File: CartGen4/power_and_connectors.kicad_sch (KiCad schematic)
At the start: 34 parts, among them J2 Conn_01x05_Male, U1 TPS65266-1RHBR

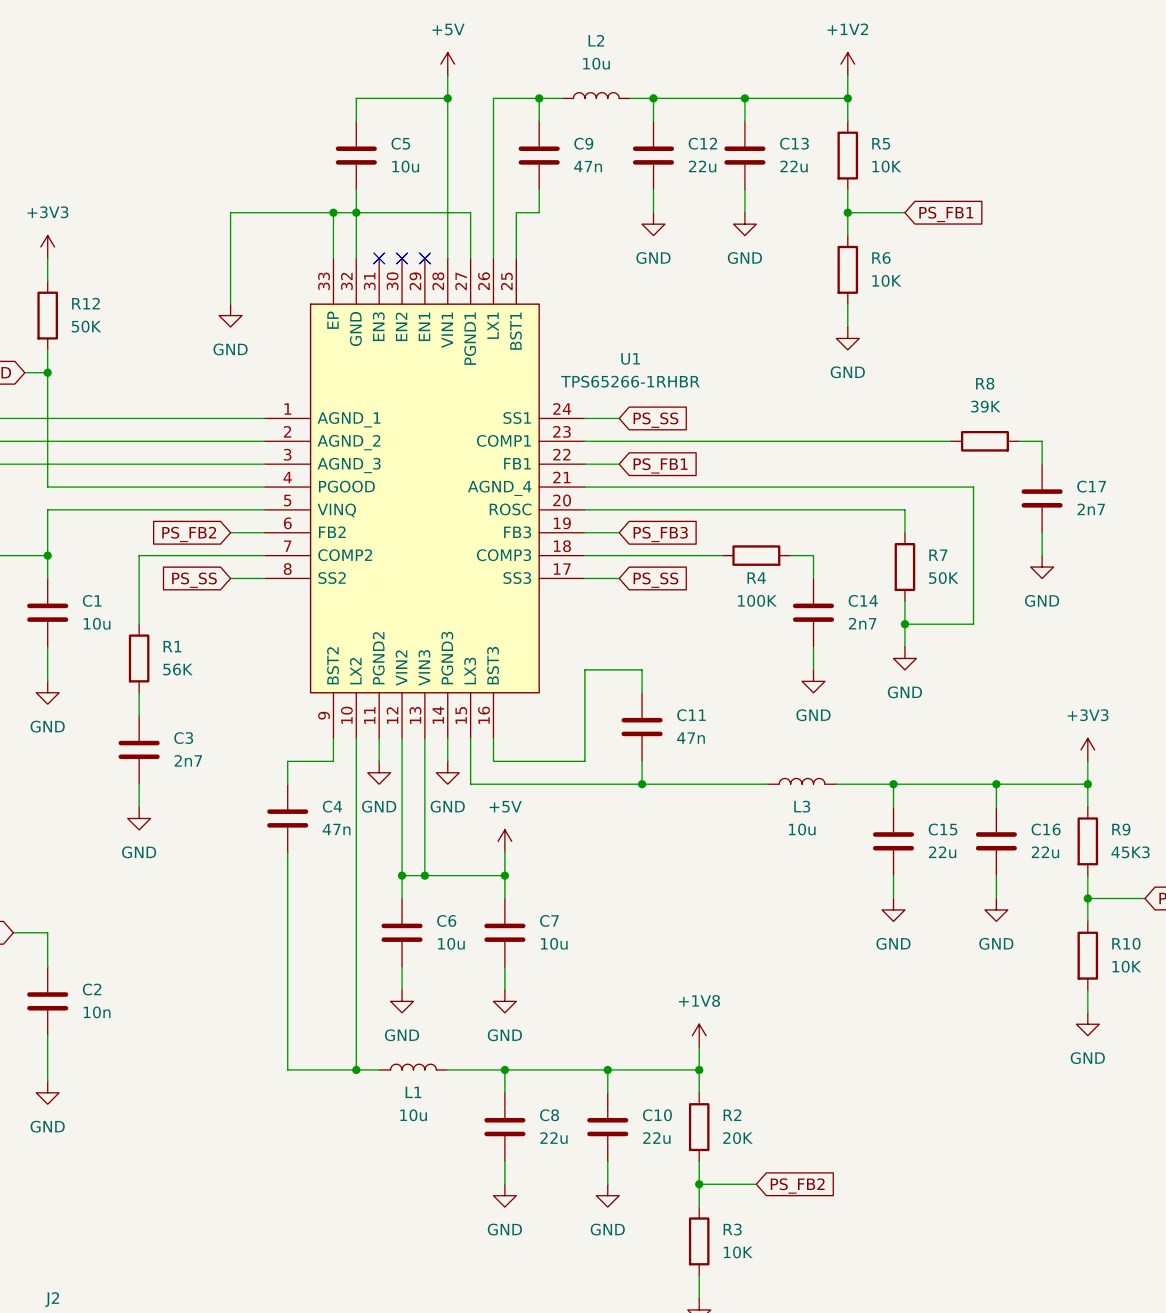
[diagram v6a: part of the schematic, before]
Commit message: Switched 1V2 and 1V8 supplies
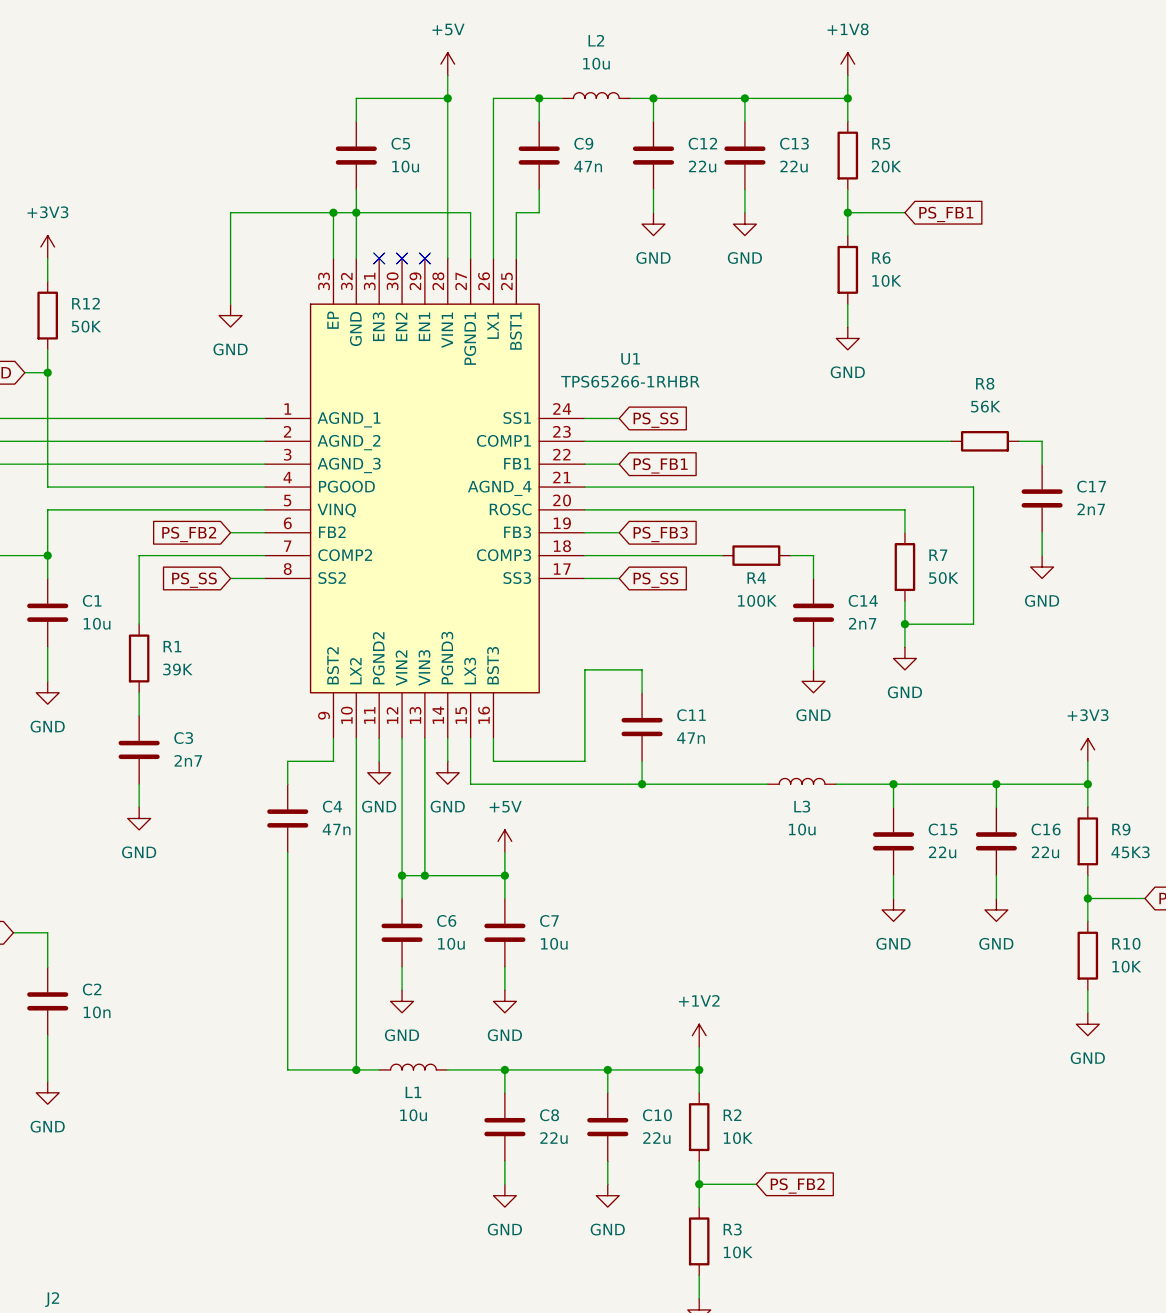
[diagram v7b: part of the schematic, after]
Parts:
- R1: value 56K -> 39K
- R2: value 20K -> 10K
- R5: value 10K -> 20K
- R8: value 39K -> 56K
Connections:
- net +1V2: now also C10.1, C8.1, L1.2, R2.1; no longer C12.1, C13.1, L2.2, R5.1
- net +1V8: now also C12.1, C13.1, L2.2, R5.1; no longer C10.1, C8.1, L1.2, R2.1
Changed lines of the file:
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@@
     (pin "2")
-  )
-  (symbol (lib_id "power:+1V8") (at 115.57 137.16 0) (unit 1)
-    (in_bom yes) (on_board yes) (fields_autoplaced)
-    (property "Reference" "#PWR016" (id 0) (at 115.57 140.97 0)
-      (effects (font (size 1.27 1.27)) hide)
-    )
-    (property "Value" "+1V8" (id 1) (at 115.57 132.08 0))
-    (property "Footprint" "" (id 2) (at 115.57 137.16 0)
-      (effects (font (size 1.27 1.27)) hide)
-    )
-    (property "Datasheet" "" (id 3) (at 115.57 137.16 0)
-      (effects (font (size 1.27 1.27)) hide)
-    )
-    (pin "1")
   )
   (symbol (lib_id "Device:C") (at 109.22 101.6 0) (unit 1)
@@
     (in_bom yes) (on_board yes) (fields_autoplaced)
     (property "Reference" "R8" (id 0) (at 147.32 63.5 90))
-    (property "Value" "39K" (id 1) (at 147.32 66.04 90))
+    (property "Value" "56K" (id 1) (at 147.32 66.04 90))
     (property "Footprint" "Resistor_SMD:R_0402_1005Metric_Pad0.72x0.64mm_HandSolder" (id 2) (at 147.32 71.628 90)
       (effects (font (size 1.27 1.27)) hide)
@@
     (pin "2")
   )
-  (symbol (lib_id "power:+1V2") (at 132.08 29.21 0) (unit 1)
-    (in_bom yes) (on_board yes) (fields_autoplaced)
-    (property "Reference" "#PWR020" (id 0) (at 132.08 33.02 0)
-      (effects (font (size 1.27 1.27)) hide)
-    )
-    (property "Value" "+1V2" (id 1) (at 132.08 24.13 0))
-    (property "Footprint" "" (id 2) (at 132.08 29.21 0)
-      (effects (font (size 1.27 1.27)) hide)
-    )
-    (property "Datasheet" "" (id 3) (at 132.08 29.21 0)
-      (effects (font (size 1.27 1.27)) hide)
-    )
-    (pin "1")
-  )
   (symbol (lib_id "power:+3V3") (at 158.75 105.41 0) (unit 1)
     (in_bom yes) (on_board yes) (fields_autoplaced)
@@
       (effects (font (size 1.27 1.27)) (justify left))
     )
-    (property "Value" "10K" (id 1) (at 134.62 39.3699 0)
+    (property "Value" "20K" (id 1) (at 134.62 39.3699 0)
       (effects (font (size 1.27 1.27)) (justify left))
     )
@@
     )
     (property "Datasheet" "" (id 3) (at 50.8 182.88 0)
+      (effects (font (size 1.27 1.27)) hide)
+    )
+    (pin "1")
+  )
+  (symbol (lib_id "power:+1V2") (at 115.57 137.16 0) (unit 1)
+    (in_bom yes) (on_board yes) (fields_autoplaced)
+    (property "Reference" "#PWR?" (id 0) (at 115.57 140.97 0)
+      (effects (font (size 1.27 1.27)) hide)
+    )
+    (property "Value" "+1V2" (id 1) (at 115.57 132.08 0))
+    (property "Footprint" "" (id 2) (at 115.57 137.16 0)
+      (effects (font (size 1.27 1.27)) hide)
+    )
+    (property "Datasheet" "" (id 3) (at 115.57 137.16 0)
       (effects (font (size 1.27 1.27)) hide)
     )
@@
     )
     (property "Datasheet" "" (id 3) (at 93.98 115.57 0)
+      (effects (font (size 1.27 1.27)) hide)
+    )
+    (pin "1")
+  )
+  (symbol (lib_id "power:+1V8") (at 132.08 29.21 0) (unit 1)
+    (in_bom yes) (on_board yes) (fields_autoplaced)
+    (property "Reference" "#PWR?" (id 0) (at 132.08 33.02 0)
+      (effects (font (size 1.27 1.27)) hide)
+    )
+    (property "Value" "+1V8" (id 1) (at 132.08 24.13 0))
+    (property "Footprint" "" (id 2) (at 132.08 29.21 0)
+      (effects (font (size 1.27 1.27)) hide)
+    )
+    (property "Datasheet" "" (id 3) (at 132.08 29.21 0)
       (effects (font (size 1.27 1.27)) hide)
     )
@@
       (effects (font (size 1.27 1.27)) (justify left))
     )
-    (property "Value" "56K" (id 1) (at 55.88 95.2499 0)
+    (property "Value" "39K" (id 1) (at 55.88 95.2499 0)
       (effects (font (size 1.27 1.27)) (justify left))
     )
@@
       (effects (font (size 1.27 1.27)) (justify left))
     )
-    (property "Value" "20K" (id 1) (at 118.11 147.3199 0)
-      (effects (font (size 1.27 1.27)) (justify left))
-    )
+    (property "Value" "10K" (id 1) (at 118.11 147.3199 0)
+      (effects (font (size 1.27 1.27)) (justify left))
+    )

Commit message: Change JTAG pins to 1mm pitch
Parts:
- J2: footprint Connector_PinHeader_2.54mm:PinHeader_1x05_P2.54mm_Horizontal -> Connector_PinHeader_1.00mm:PinHeader_1x05_P1.00mm_Vertical
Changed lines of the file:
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@@
   (symbol (lib_id "power:+1V2") (at 115.57 137.16 0) (unit 1)
     (in_bom yes) (on_board yes) (fields_autoplaced)
-    (property "Reference" "#PWR?" (id 0) (at 115.57 140.97 0)
+    (property "Reference" "#PWR0110" (id 0) (at 115.57 140.97 0)
       (effects (font (size 1.27 1.27)) hide)
     )
@@
     (property "Reference" "J2" (id 0) (at 43.815 165.1 0))
     (property "Value" "Conn_01x05_Male" (id 1) (at 43.815 167.64 0))
-    (property "Footprint" "Connector_PinHeader_2.54mm:PinHeader_1x05_P2.54mm_Horizontal" (id 2) (at 43.18 175.26 0)
+    (property "Footprint" "Connector_PinHeader_1.00mm:PinHeader_1x05_P1.00mm_Vertical" (id 2) (at 43.18 175.26 0)
       (effects (font (size 1.27 1.27)) hide)
     )
@@
   (symbol (lib_id "power:+1V8") (at 132.08 29.21 0) (unit 1)
     (in_bom yes) (on_board yes) (fields_autoplaced)
-    (property "Reference" "#PWR?" (id 0) (at 132.08 33.02 0)
-      (effects (font (size 1.27 1.27)) hide)
-    )
+    (property "Reference" "#PWR0111" (id 0) (at 132.08 33.02 0)
+      (effects (font (size 1.27 1.27)) hide)
+    )
